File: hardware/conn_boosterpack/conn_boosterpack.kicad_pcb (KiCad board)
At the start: 2 copper layers, 50.8 x 30.5 mm, 10 parts, among them J1 Conn_01x08, J2 Conn_01x08, J3 Conn_01x40

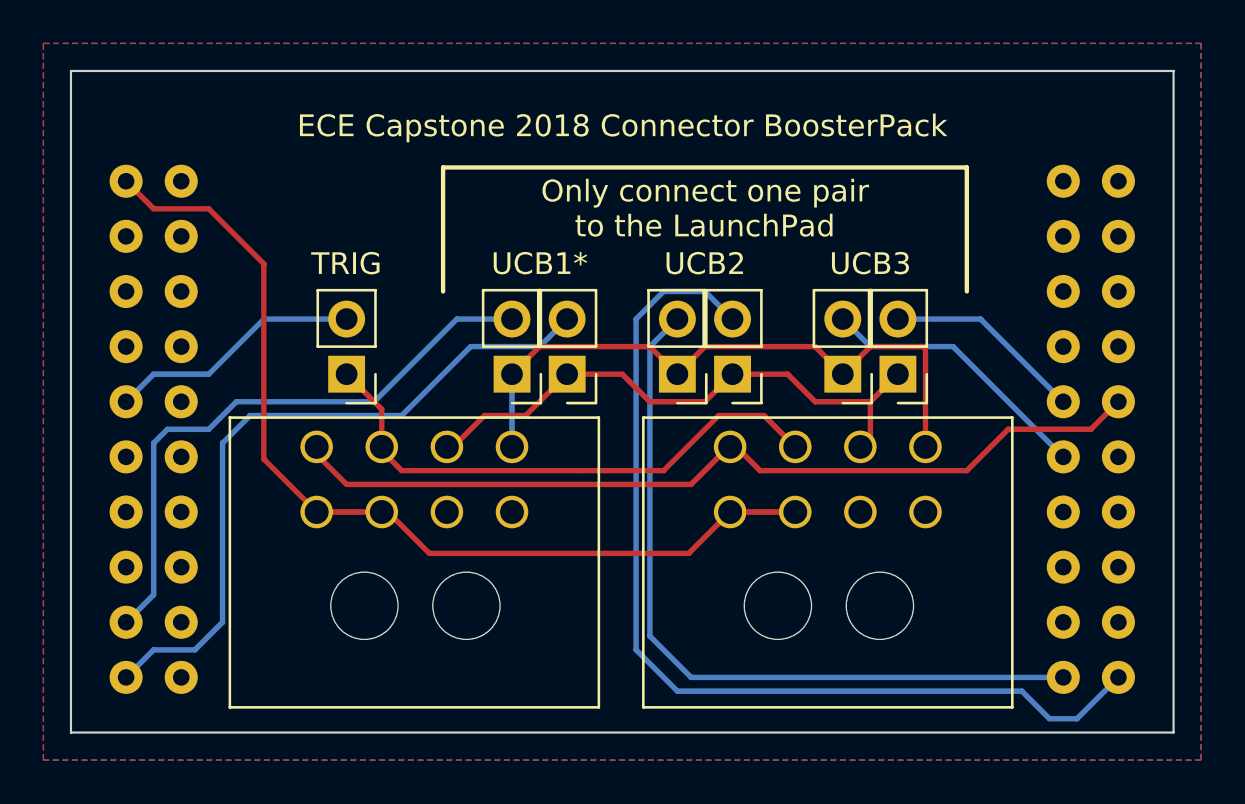
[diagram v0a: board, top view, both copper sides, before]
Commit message: Fixed hole sizes (ugh)
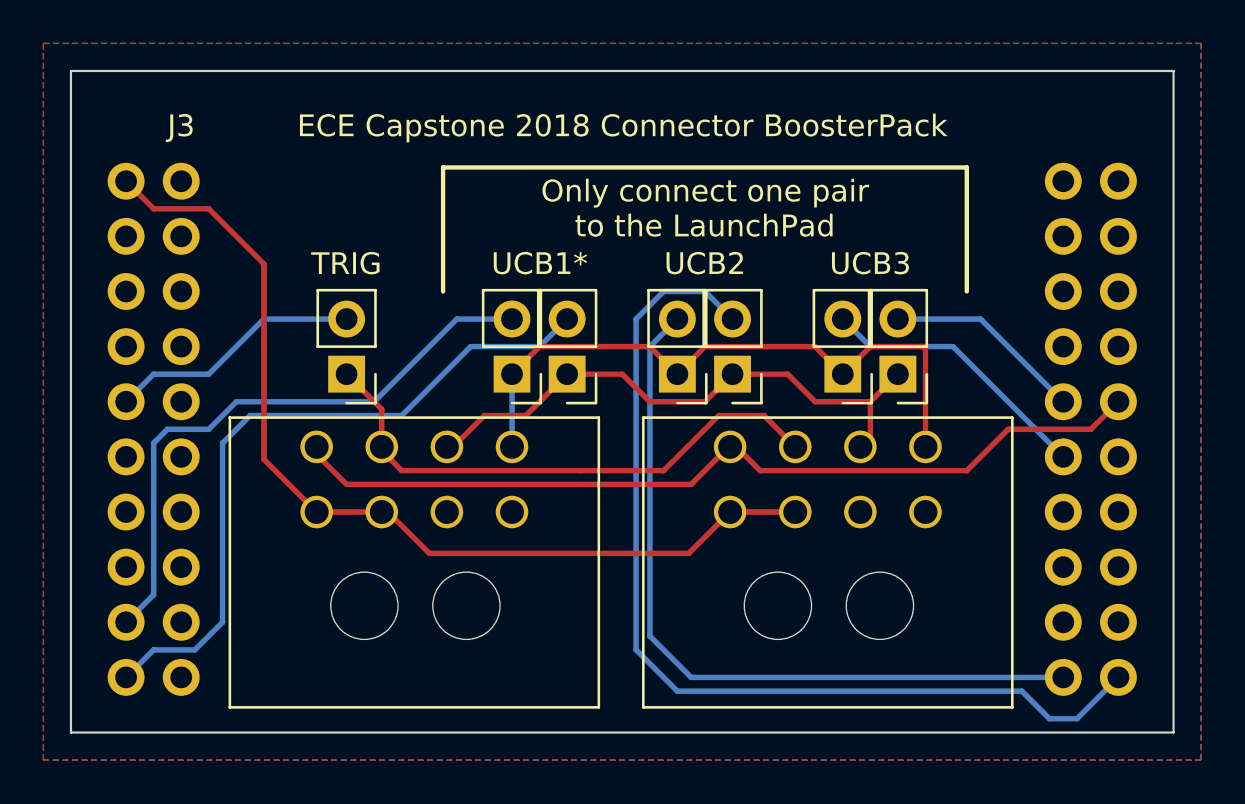
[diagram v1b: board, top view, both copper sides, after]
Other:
- board text added: "Ag Despopoulos Version 3"
- board text removed: "Ag Despopoulos Version 2"
